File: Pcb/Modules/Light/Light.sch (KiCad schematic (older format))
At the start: 19 parts, among them J1 JACK_RJ45, J2 JACK_STEREO, Q1 TEPT4400, Q2 Q_NMOS_GSD, U1 74LVC1G07, U2 74LVC1G07

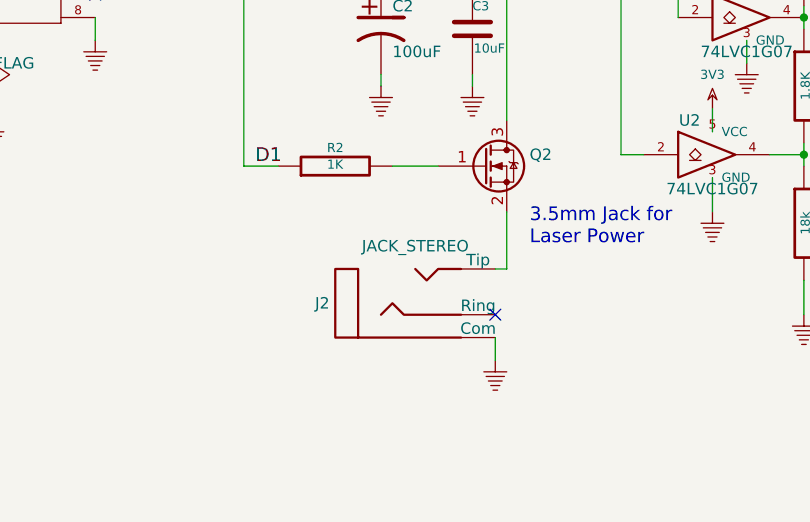
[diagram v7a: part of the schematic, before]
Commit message: Add pulldown resistor to light module.  Add laser off/on control to light menu
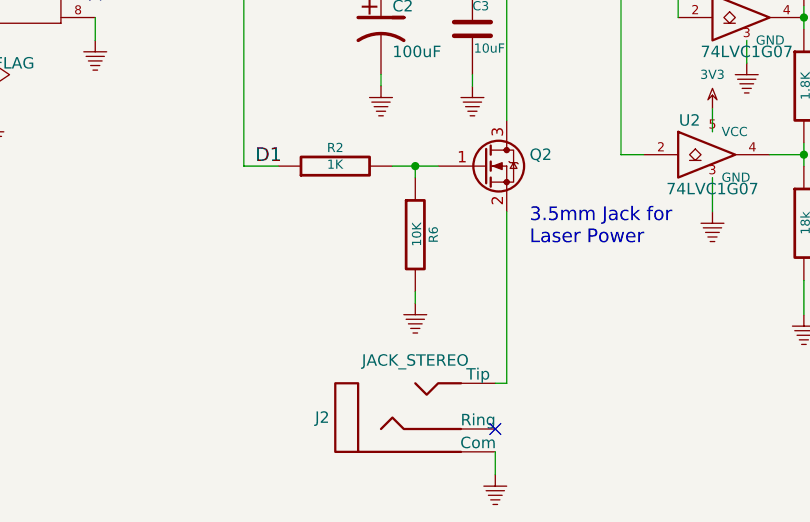
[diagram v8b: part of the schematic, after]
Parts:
- added R6: 10K, CA6:SM0603_Resistor, symbol R
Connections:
- net GND: now also R6.2
- net at Q2.1 (G), R2.2: now also R6.1
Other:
- moved on the sheet: J2
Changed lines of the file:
@@
 L JACK_STEREO J2
 U 1 1 54012E4D
-P 6050 5250
-F 0 "J2" H 5675 5250 50  0000 R CNN
-F 1 "JACK_STEREO" H 6050 5500 50  0000 C CNN
-F 2 "CA6:161-3334-E_Big_Pad" H 6050 5250 60  0001 C CNN
-F 3 "~" H 6050 5250 60  0000 C CNN
-	1    6050 5250
+P 6050 5750
+F 0 "J2" H 5675 5750 50  0000 R CNN
+F 1 "JACK_STEREO" H 6050 6000 50  0000 C CNN
+F 2 "CA6:161-3334-E_Big_Pad" H 6050 5750 60  0001 C CNN
+F 3 "~" H 6050 5750 60  0000 C CNN
+	1    6050 5750
 	1    0    0    -1
 $EndComp
@@
 $EndComp
 $Comp
-L 3V3 #PWR01
+L 3V3 #PWR3
 U 1 1 540144B1
 P 4650 3200
-F 0 "#PWR01" H 4650 3300 40  0001 C CNN
+F 0 "#PWR3" H 4650 3300 40  0001 C CNN
 F 1 "3V3" H 4650 3325 40  0000 C CNN
 F 2 "" H 4650 3200 60  0000 C CNN
@@
 D5
 $Comp
-L GND #PWR02
+L GND #PWR4
 U 1 1 540144C2
 P 4650 4100
-F 0 "#PWR02" H 4650 4100 30  0001 C CNN
+F 0 "#PWR4" H 4650 4100 30  0001 C CNN
 F 1 "GND" H 4650 4030 30  0001 C CNN
 F 2 "" H 4650 4100 60  0000 C CNN
@@
 	4650 3200 4650 3300
 $Comp
-L 3V3 #PWR03
+L 3V3 #PWR7
 U 1 1 5401450D
 P 5800 3800
-F 0 "#PWR03" H 5800 3900 40  0001 C CNN
+F 0 "#PWR7" H 5800 3900 40  0001 C CNN
 F 1 "3V3" H 5800 3925 40  0000 C CNN
 F 2 "" H 5800 3800 60  0000 C CNN
@@
 	0    -1   1    0
 $EndComp
-$Comp
-L GND #PWR04
-U 1 1 5401451B
-P 6400 5500
-F 0 "#PWR04" H 6400 5500 30  0001 C CNN
-F 1 "GND" H 6400 5430 30  0001 C CNN
-F 2 "" H 6400 5500 60  0000 C CNN
-F 3 "" H 6400 5500 60  0000 C CNN
-	1    6400 5500
-	1    0    0    -1
-$EndComp
-Wire Wire Line
-	6400 5400 6400 5500
 Wire Wire Line
 	4650 4000 4650 4100
@@
 $EndComp
 $Comp
-L 3V3 #PWR05
+L 3V3 #PWR6
 U 1 1 54AA199D
 P 5750 2750
-F 0 "#PWR05" H 5750 2850 40  0001 C CNN
+F 0 "#PWR6" H 5750 2850 40  0001 C CNN
 F 1 "3V3" H 5750 2875 40  0000 C CNN
 F 2 "" H 5750 2750 60  0000 C CNN
@@
 $EndComp
 $Comp
-L GND #PWR06
+L GND #PWR16
 U 1 1 54AA1A1B
 P 7750 5300
-F 0 "#PWR06" H 7750 5300 30  0001 C CNN
+F 0 "#PWR16" H 7750 5300 30  0001 C CNN
 F 1 "GND" H 7750 5230 30  0001 C CNN
 F 2 "" H 7750 5300 60  0000 C CNN
@@
 $EndComp
 $Comp
-L GND #PWR07
+L GND #PWR5
 U 1 1 54AABCE0
 P 5250 3100
-F 0 "#PWR07" H 5250 3100 30  0001 C CNN
+F 0 "#PWR5" H 5250 3100 30  0001 C CNN
 F 1 "GND" H 5250 3030 30  0001 C CNN
 F 2 "" H 5250 3100 60  0000 C CNN
@@
 NoConn ~ 4650 3800
 NoConn ~ 4650 3900
-NoConn ~ 6400 5300
-$Comp
-L PWR_FLAG #FLG08
+NoConn ~ 6400 5800
+$Comp
+L PWR_FLAG #FLG2
 U 1 1 58FEFDE5
 P 4300 2950
-F 0 "#FLG08" H 4300 3025 50  0001 C CNN
+F 0 "#FLG2" H 4300 3025 50  0001 C CNN
 F 1 "PWR_FLAG" H 4300 3100 50  0000 C CNN
 F 2 "" H 4300 2950 50  0001 C CNN
@@
 $EndComp
 $Comp
-L 3V3 #PWR09
+L 3V3 #PWR2
 U 1 1 58FEFE63
 P 4300 2850
-F 0 "#PWR09" H 4300 2950 40  0001 C CNN
+F 0 "#PWR2" H 4300 2950 40  0001 C CNN
 F 1 "3V3" H 4300 2975 40  0000 C CNN
 F 2 "" H 4300 2850 60  0000 C CNN
@@
 	6150 4650 5950 4650
 Wire Wire Line
-	6450 4850 6450 5100
-Wire Wire Line
-	6450 5100 6400 5100
+	6450 4850 6450 5600
 Wire Wire Line
 	5300 4650 5450 4650
@@
 R2 for MAX current of 20mA\n(3.3V - .17 drop across Buffer)/20mA=156.5 ohms\nUse 160 ohms for max current = 19.5 mA
 $Comp
-L PWR_FLAG #FLG010
+L PWR_FLAG #FLG1
 U 1 1 59E23186
 P 4200 4350
-F 0 "#FLG010" H 4200 4425 50  0001 C CNN
+F 0 "#FLG1" H 4200 4425 50  0001 C CNN
 F 1 "PWR_FLAG" H 4200 4500 50  0000 C CNN
 F 2 "" H 4200 4350 50  0001 C CNN
@@
 $EndComp
 $Comp
-L GND #PWR011
+L GND #PWR1
 U 1 1 59E231B3
 P 4200 4450
-F 0 "#PWR011" H 4200 4450 30  0001 C CNN
+F 0 "#PWR1" H 4200 4450 30  0001 C CNN
 F 1 "GND" H 4200 4380 30  0001 C CNN
 F 2 "" H 4200 4450 60  0000 C CNN
@@
 	6950 3700 4650 3700
 $Comp
-L GND #PWR012
+L GND #PWR13
 U 1 1 5A247E92
 P 7350 4850
-F 0 "#PWR012" H 7350 4850 30  0001 C CNN
+F 0 "#PWR13" H 7350 4850 30  0001 C CNN
 F 1 "GND" H 7350 4780 30  0001 C CNN
 F 2 "" H 7350 4850 60  0000 C CNN
@@
 $EndComp
 $Comp
-L GND #PWR013
+L GND #PWR15
 U 1 1 5A247ECA
 P 7500 4200
-F 0 "#PWR013" H 7500 4200 30  0001 C CNN
+F 0 "#PWR15" H 7500 4200 30  0001 C CNN
 F 1 "GND" H 7500 4130 30  0001 C CNN
 F 2 "" H 7500 4200 60  0000 C CNN
@@
 $EndComp
 $Comp
-L 3V3 #PWR014
+L 3V3 #PWR14
 U 1 1 5A248403
 P 7500 3800
-F 0 "#PWR014" H 7500 3900 40  0001 C CNN
+F 0 "#PWR14" H 7500 3900 40  0001 C CNN
 F 1 "3V3" H 7500 3925 40  0000 C CNN
 F 2 "" H 7500 3800 60  0000 C CNN
@@
 $EndComp
 $Comp
-L 3V3 #PWR015
+L 3V3 #PWR12
 U 1 1 5A2484A4
 P 7350 4400
-F 0 "#PWR015" H 7350 4500 40  0001 C CNN
+F 0 "#PWR12" H 7350 4500 40  0001 C CNN
 F 1 "3V3" H 7350 4550 40  0000 C CNN
 F 2 "" H 7350 4400 60  0000 C CNN
@@
 Connection ~ 5900 3800
 $Comp
-L GND #PWR016
+L GND #PWR8
 U 1 1 5A2880E8
 P 5900 4300
-F 0 "#PWR016" H 5900 4300 30  0001 C CNN
+F 0 "#PWR8" H 5900 4300 30  0001 C CNN
 F 1 "GND" H 5900 4230 30  0001 C CNN
 F 2 "" H 5900 4300 60  0000 C CNN
@@
 $EndComp
 $Comp
-L GND #PWR017
+L GND #PWR10
 U 1 1 5A288126
 P 6300 4300
-F 0 "#PWR017" H 6300 4300 30  0001 C CNN
+F 0 "#PWR10" H 6300 4300 30  0001 C CNN
 F 1 "GND" H 6300 4230 30  0001 C CNN
 F 2 "" H 6300 4300 60  0000 C CNN
@@
 	1    0    0    -1
 $EndComp
+$Comp
+L GND #PWR11
+U 1 1 5401451B
+P 6400 6000
+F 0 "#PWR11" H 6400 6000 30  0001 C CNN
+F 1 "GND" H 6400 5930 30  0001 C CNN
+F 2 "" H 6400 6000 60  0000 C CNN
+F 3 "" H 6400 6000 60  0000 C CNN
+	1    6400 6000
+	1    0    0    -1
+$EndComp
+Wire Wire Line
+	6400 5900 6400 6000
+Wire Wire Line
+	6450 5600 6400 5600
+$Comp
+L R R6
+U 1 1 5A32AF14
+P 6050 4950
+F 0 "R6" V 6130 4950 40  0000 C CNN
+F 1 "10K" V 6057 4951 40  0000 C CNN
+F 2 "CA6:SM0603_Resistor" V 5980 4950 30  0001 C CNN
+F 3 "~" H 6050 4950 30  0000 C CNN
+	1    6050 4950
+	1    0    0    -1
+$EndComp
+Wire Wire Line
+	6050 4700 6050 4650
+Connection ~ 6050 4650
+$Comp
+L GND #PWR9
+U 1 1 5A32B0B2
+P 6050 5250
+F 0 "#PWR9" H 6050 5250 30  0001 C CNN
+F 1 "GND" H 6050 5180 30  0001 C CNN
+F 2 "" H 6050 5250 60  0000 C CNN
+F 3 "" H 6050 5250 60  0000 C CNN
+	1    6050 5250
+	1    0    0    -1
+$EndComp
+Wire Wire Line
+	6050 5250 6050 5200
 $EndSCHEMATC
